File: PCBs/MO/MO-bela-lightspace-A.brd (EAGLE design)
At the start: 63.5 x 63.2 mm, 14 parts

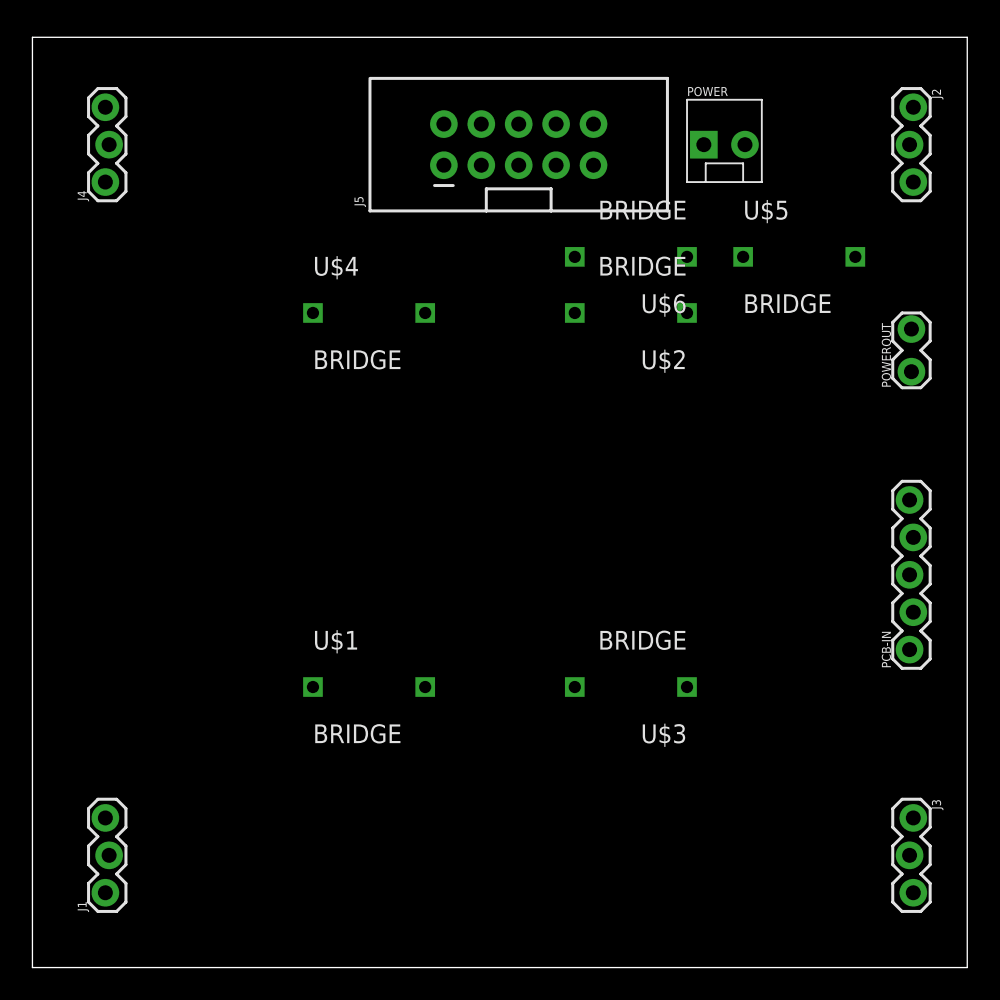
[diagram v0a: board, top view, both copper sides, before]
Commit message: lightbox for bela
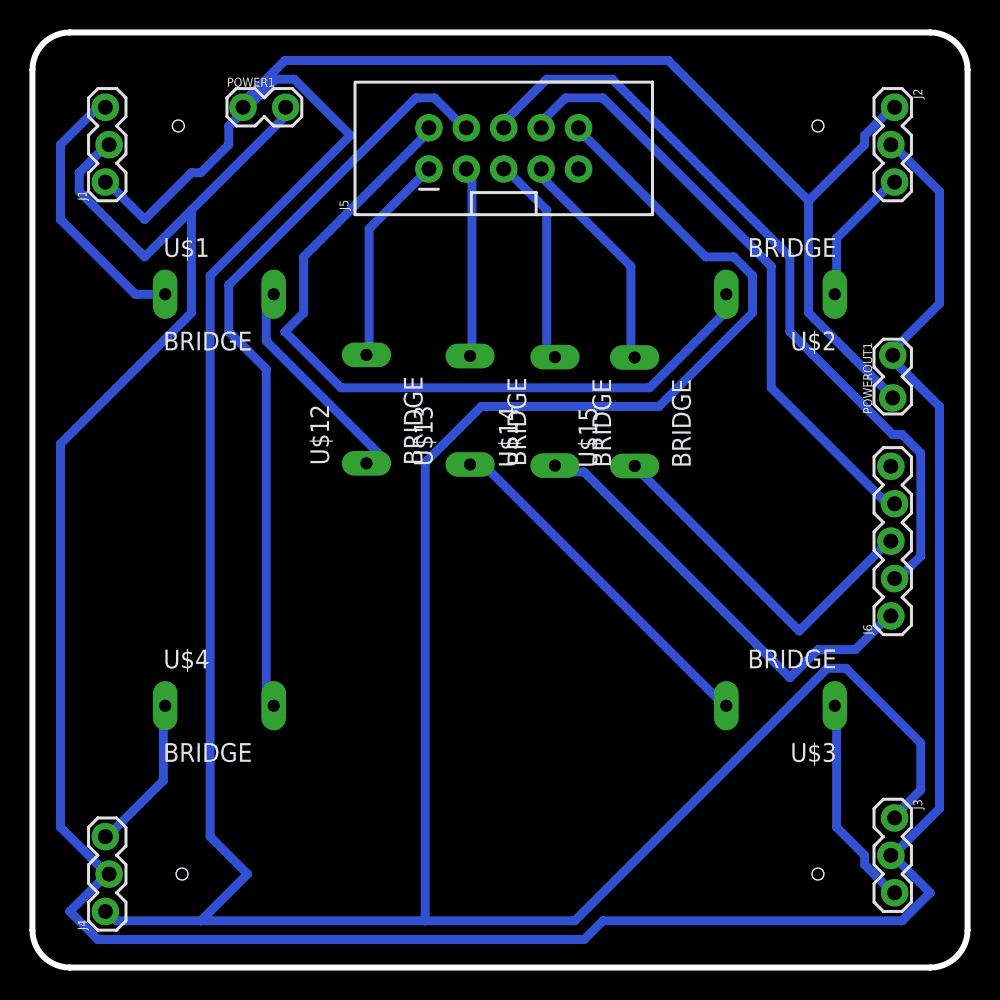
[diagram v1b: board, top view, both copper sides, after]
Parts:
- removed PCB-IN: (no value), SparkFun-Connectors:1X05_LOCK
- removed POWER: (no value), SparkFun-Connectors:MOLEX-1X2_LOCK
- removed POWEROUT: (no value), SparkFun-Connectors:1X02_LOCK
- removed U$5, U$6: BRIDGE, CMU-ArtFab:BRIDGE
- added J6: (no value), SparkFun-Connectors:1X05_LOCK
- added POWER1, POWEROUT1: (no value), SparkFun-Connectors:1X02_LOCK
- added U$12, U$13, U$14, U$15: BRIDGE, CMU-ArtFab:BRIDGE
- moved J4 49.5 mm to (5.08, 3.81)
- moved J1 48.3 mm to (5.08, 53.3)
- moved U$4 27.4 mm to (12.7, 17.8)
- moved U$1 27.4 mm to (12.7, 45.7)
- moved U$3 6.48 mm to (50.8, 17.8)
- moved U$2 6.48 mm to (50.8, 45.7)
- moved J2 1.27 mm to (58.4, 58.4)
- moved J3 1.27 mm to (58.4, 10.2)
- moved J5 1.05 mm to (32.0, 55.6)
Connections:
- removed net N$5: J5.9
- removed net N$6: POWER.2, U$5.P$1
- removed net N$7: POWER.1, U$6.P$1
- new net N$10: J5.5, U$14.P$2
- new net N$11: J5.7, U$15.P$2
- new net N$8: J5.1, U$12.P$2
- new net N$9: J5.3, U$13.P$2
- net AMBI1: now also U$12.P$1; no longer J5.1
- net AMBI1A: now also J6.1, U$14.P$1; no longer J5.5, PCB-IN.1
- net AMBI2A: now also J6.2; no longer PCB-IN.2
- net AMBI3: now also U$13.P$1; no longer J5.3
- net AMBI3A: now also J6.3, U$15.P$1; no longer J5.7, PCB-IN.3
- net AMBI4A: now also J6.4; no longer PCB-IN.4
- net GND: now also POWER1.1, POWEROUT1.1; no longer POWEROUT.1, U$6.P$2
- net VCC: now also POWER1.2, POWEROUT1.2; no longer POWEROUT.2, U$5.P$2
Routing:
- net GND: track 0.00 -> 299.2 mm
- net VCC: track 0.00 -> 197.0 mm
- net AMBI2A: track 0.00 -> 52.9 mm
- net AMBI2: track 0.00 -> 52.8 mm
- net AMBI4: track 0.00 -> 52.3 mm
- net AMBI4A: track 0.00 -> 41.9 mm
- net AMBI1A: track 0.00 -> 30.7 mm
- net AMBI3: track 0.00 -> 24.9 mm
- net AMBI3A: track 0.00 -> 24.5 mm
- net N$1: track 0.00 -> 18.4 mm
- net N$11: track 0.00 -> 15.6 mm
- net AMBI1: track 0.00 -> 15.5 mm
- net N$3: track 0.00 -> 14.5 mm
- net N$8: track 0.00 -> 14.4 mm
- net N$10: track 0.00 -> 14.3 mm
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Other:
- board size 63.5 x 63.2 mm -> 63.5 x 63.5 mm
